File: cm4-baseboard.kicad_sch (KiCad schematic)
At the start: 4 parts

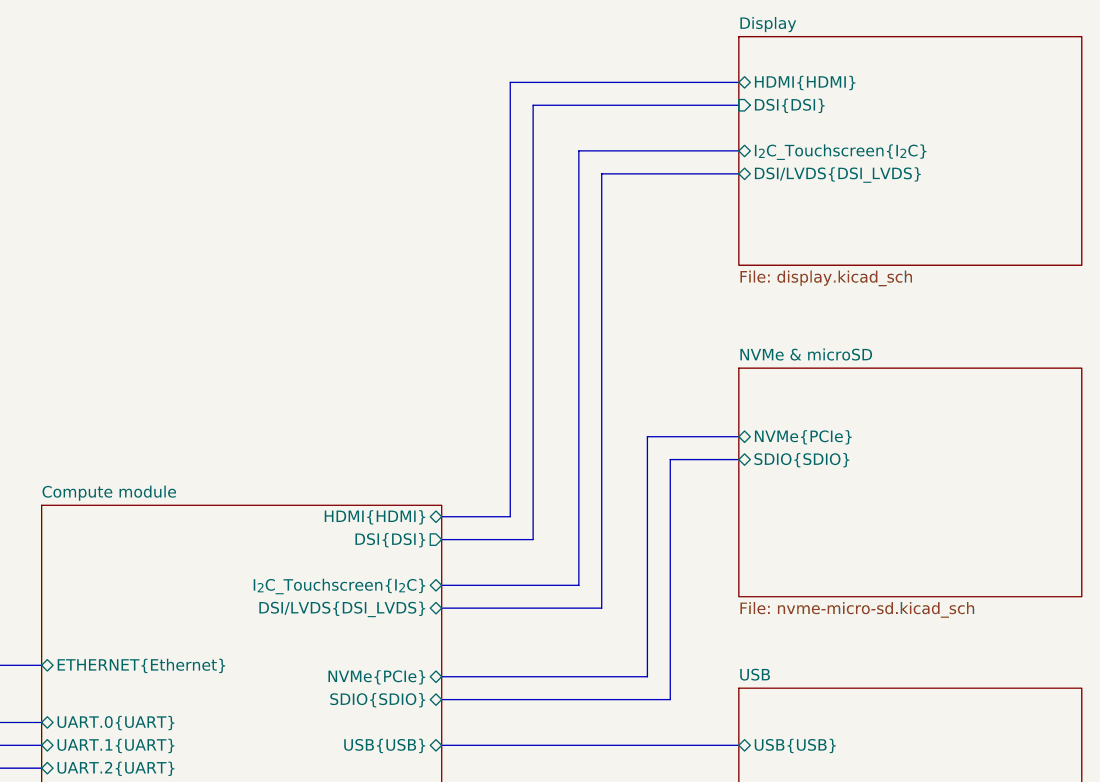
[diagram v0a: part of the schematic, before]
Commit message: [#54231] Rename bus DSI/LVDS to DisplayCtrl
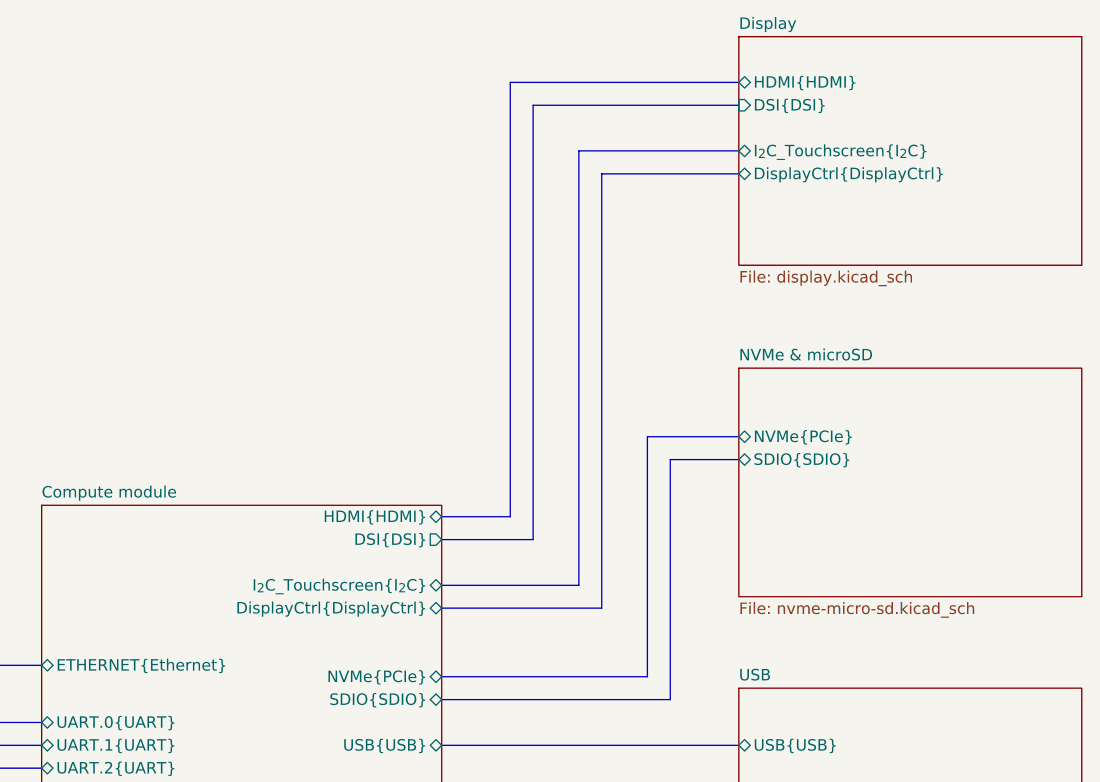
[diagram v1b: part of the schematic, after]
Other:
- sheet Compute module ports: added DisplayCtrl{DisplayCtrl}; removed DSI/LVDS{DSI_LVDS}
- sheet Display ports: added DisplayCtrl{DisplayCtrl}; removed DSI/LVDS{DSI_LVDS}
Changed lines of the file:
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@@
   (bus_alias "CSI" (members "D0_P" "D0_N" "D1_P" "D1_N" "D2_P" "D2_N" "D3_P" "D3_N" "CLK_P" "CLK_N"))
   (bus_alias "PCIe" (members "TX0_P" "TX0_N" "RX0_P" "RX0_N" "CLK_P" "CLK_N" "TX1_N" "TX2_N" "TX3_N" "TX1_P" "TX2_P" "TX3_P" "RX1_N" "RX2_N" "RX3_N" "RX1_P" "RX2_P" "RX3_P" "~{RST}" "~{CLK_REQ}"))
-  (bus_alias "HDMI" (members "D0_P" "D0_N" "D1_P" "D1_N" "D2_P" "D2_N" "CLK_P" "CLK_N" "SCL" "SDA" "CEC" "HPD"))
+  (bus_alias "SDIO" (members "D0" "D1" "D2" "D3" "CMD" "CLK" "CD"))
   (bus_alias "Ethernet" (members "D0_P" "D0_N" "D1_P" "D1_N" "D2_P" "D2_N" "D3_P" "D3_N" "LED_ACT" "LED_LINK"))
   (bus_alias "I_{2}C" (members "SCL" "SDA"))
-  (bus_alias "UART" (members "TX" "RX"))
   (bus_alias "USB" (members "RX_P" "RX_N" "TX_P" "TX_N" "D_P" "D_N"))
+  (bus_alias "HDMI" (members "D0_P" "D0_N" "D1_P" "D1_N" "D2_P" "D2_N" "CLK_P" "CLK_N" "SCL" "SDA" "CEC" "HPD"))
+  (bus_alias "UART" (members "TX" "RX"))
   (bus_alias "DSI" (members "D0_P" "D0_N" "D1_P" "D1_N" "D2_P" "D2_N" "D3_P" "D3_N" "CLK_P" "CLK_N"))
-  (bus_alias "SDIO" (members "D0" "D1" "D2" "D3" "CMD" "CLK" "CD"))
   (junction (at 166.37 264.16) (diameter 0) (color 0 0 0 0)
   )
@@
       (effects (font (size 1.27 1.27)) (justify right))
     )
-    (pin "DSI{slash}LVDS{DSI_LVDS}" bidirectional (at 243.84 113.03 0)
+    (pin "DisplayCtrl{DisplayCtrl}" bidirectional (at 243.84 113.03 0)
       (effects (font (size 1.27 1.27)) (justify right))
     )
@@
       (effects (font (size 1.27 1.27)) (justify left))
     )
-    (pin "DSI{slash}LVDS{DSI_LVDS}" bidirectional (at 276.86 64.77 180)
+    (pin "DisplayCtrl{DisplayCtrl}" bidirectional (at 276.86 64.77 180)
       (effects (font (size 1.27 1.27)) (justify left))
     )
@@
       (reference "#PWR?") (unit 1) (value "GND") (footprint "")
     )
-    (path "/b148dc70-7270-4ae3-80a1-580624d4cd31/5d61928f-81f0-4a4c-b452-b4734d3ec233/341a8429-1a92-49c6-adcc-ef7f1edcb952"
-      (reference "#PWR?") (unit 1) (value "GND") (footprint "")
-    )
     (path "/db597aea-6022-4be8-a5d9-f0f6712c4ff6/3813b611-ae52-4008-8362-850e3aa20b82"
       (reference "#PWR?") (unit 1) (value "GND") (footprint "")
@@
       (reference "#PWR?") (unit 1) (value "GND") (footprint "")
     )
-    (path "/b148dc70-7270-4ae3-80a1-580624d4cd31/5d61928f-81f0-4a4c-b452-b4734d3ec233/9a1114cc-d9e5-4f03-8637-8d3b91b40497"
-      (reference "#PWR?") (unit 1) (value "GND") (footprint "")
-    )
     (path "/00000000-0000-0000-0000-00005fea17c4/9cdec078-c17e-4daa-b8f1-7b28647f66b6"
       (reference "#PWR?") (unit 1) (value "+1V8") (footprint "")
@@
       (reference "C?") (unit 1) (value "C_template_name_0402") (footprint "antmicro-footprints:C_0402_1005Metric")
     )
+    (path "/b148dc70-7270-4ae3-80a1-580624d4cd31/5d61928f-81f0-4a4c-b452-b4734d3ec233/257eb24e-a684-4d63-8a65-0f0a78448243"
+      (reference "C?") (unit 1) (value "C_22u_25V_0805") (footprint "antmicro-footprints:C_0805_2012Metric")
+    )
     (path "/db597aea-6022-4be8-a5d9-f0f6712c4ff6/274e8c82-a4a9-46ce-bc84-d16e09bbd0c9"
       (reference "C?") (unit 1) (value "C_template_name_0402") (footprint "antmicro-footprints:C_0402_1005Metric")
@@
       (reference "C?") (unit 1) (value "C_330n_0603") (footprint "antmicro-footprints:C_0603_1608Metric")
     )
-    (path "/b148dc70-7270-4ae3-80a1-580624d4cd31/5d61928f-81f0-4a4c-b452-b4734d3ec233/453fe00b-ff52-4ef4-ba8f-d2d782db81e2"
-      (reference "C?") (unit 1) (value "C_10u_25V_0603") (footprint "antmicro-footprints:C_0603_1608Metric")
-    )
     (path "/00000000-0000-0000-0000-00005fea17e9/482637d7-45a3-440c-a11b-ab27ad2a09ba"
       (reference "C?") (unit 1) (value "C_22u_25V_0805") (footprint "antmicro-footprints:C_0805_2012Metric")
@@
       (reference "C?") (unit 1) (value "C_template_name_0402") (footprint "antmicro-footprints:C_0402_1005Metric")
     )
-    (path "/b148dc70-7270-4ae3-80a1-580624d4cd31/5d61928f-81f0-4a4c-b452-b4734d3ec233/5d833b9e-85a4-4a6f-8684-1cf9bdef1f01"
-      (reference "C?") (unit 1) (value "C_10u_25V_0603") (footprint "antmicro-footprints:C_0603_1608Metric")
-    )
-    (path "/b148dc70-7270-4ae3-80a1-580624d4cd31/5d61928f-81f0-4a4c-b452-b4734d3ec233/66dfef94-3e33-403a-b2be-3a327f56dc92"
-      (reference "C?") (unit 1) (value "C_10u_25V_0603") (footprint "antmicro-footprints:C_0603_1608Metric")
-    )
     (path "/00000000-0000-0000-0000-00005fea17e9/6b7d1f22-0be8-47c7-b016-6d7c031b8b41"
       (reference "C?") (unit 1) (value "C_22u_25V_0805") (footprint "antmicro-footprints:C_0805_2012Metric")
@@
       (reference "C?") (unit 1) (value "C_100n_0402") (footprint "antmicro-footprints:C_0402_1005Metric")
     )
-    (path "/b148dc70-7270-4ae3-80a1-580624d4cd31/5d61928f-81f0-4a4c-b452-b4734d3ec233/75197a1d-780f-46d2-9dce-65e41d058c74"
-      (reference "C?") (unit 1) (value "C_10u_25V_0603") (footprint "antmicro-footprints:C_0603_1608Metric")
-    )
     (path "/00000000-0000-0000-0000-00005fea17e9/780dfd9c-fc8c-4089-8330-e7de2f742555"
       (reference "C?") (unit 1) (value "C_22u_25V_0805") (footprint "antmicro-footprints:C_0805_2012Metric")
@@
       (reference "C?") (unit 1) (value "C_100n_0402") (footprint "antmicro-footprints:C_0402_1005Metric")
     )
+    (path "/b148dc70-7270-4ae3-80a1-580624d4cd31/5d61928f-81f0-4a4c-b452-b4734d3ec233/7b087682-4398-4ae5-9794-83c9bb11e283"
+      (reference "C?") (unit 1) (value "C_22u_25V_0805") (footprint "antmicro-footprints:C_0805_2012Metric")
+    )
     (path "/b148dc70-7270-4ae3-80a1-580624d4cd31/5d61928f-81f0-4a4c-b452-b4734d3ec233/80d05272-f4bc-4c0b-b517-a6d34f4a8421"
       (reference "C?") (unit 1) (value "C_1u_25V_0402") (footprint "antmicro-footprints:C_0402_1005Metric")
@@
       (reference "C?") (unit 1) (value "C_10p_0402") (footprint "antmicro-footprints:C_0402_1005Metric")
     )
+    (path "/b148dc70-7270-4ae3-80a1-580624d4cd31/5d61928f-81f0-4a4c-b452-b4734d3ec233/87418403-96e0-4834-9247-2518b8abc38b"
+      (reference "C?") (unit 1) (value "C_22u_25V_0805") (footprint "antmicro-footprints:C_0805_2012Metric")
+    )
     (path "/db597aea-6022-4be8-a5d9-f0f6712c4ff6/88d5e9a9-c2b1-463d-919b-768178eb5b8b"
       (reference "C?") (unit 1) (value "C_100n_0402") (footprint "antmicro-footprints:C_0402_1005Metric")
@@
       (reference "C?") (unit 1) (value "C_10n_0402") (footprint "antmicro-footprints:C_0402_1005Metric")
     )
-    (path "/b148dc70-7270-4ae3-80a1-580624d4cd31/5d61928f-81f0-4a4c-b452-b4734d3ec233/ba404e87-ab9c-4537-886b-3e04a5eb8c72"
-      (reference "C?") (unit 1) (value "C_22u_16V_0603") (footprint "antmicro-footprints:C_0603_1608Metric")
-    )
     (path "/00000000-0000-0000-0000-00005fea17e9/bc26d64c-8cd8-4a33-894b-b2b889e6c4f9"
       (reference "C?") (unit 1) (value "C_22u_25V_0805") (footprint "antmicro-footprints:C_0805_2012Metric")
@@
       (reference "C?") (unit 1) (value "C_220n_16V_0402") (footprint "antmicro-footprints:C_0402_1005Metric")
     )
+    (path "/b148dc70-7270-4ae3-80a1-580624d4cd31/5d61928f-81f0-4a4c-b452-b4734d3ec233/e050934f-2e7f-4d1d-a6b0-f09cd3270d46"
+      (reference "C?") (unit 1) (value "C_22u_25V_0805") (footprint "antmicro-footprints:C_0805_2012Metric")
+    )
     (path "/db597aea-6022-4be8-a5d9-f0f6712c4ff6/e5121825-db13-4ea1-a393-845e0e43bef6"
       (reference "C?") (unit 1) (value "C_template_name_0402") (footprint "antmicro-footprints:C_0402_1005Metric")
@@
       (reference "L1") (unit 1) (value "L_1u8_14A_Coilcraft-XAL6030") (footprint "antmicro-footprints:L_Coilcraft-XAL6030")
     )
+    (path "/b148dc70-7270-4ae3-80a1-580624d4cd31/5d61928f-81f0-4a4c-b452-b4734d3ec233/2db4c736-e13c-47a7-9ea7-9867d69cfe2b"
+      (reference "L?") (unit 1) (value "L_15u_2.8A_Coilcraft-XAL4040") (footprint "antmicro-footprints:L_Coilcraft-XAL4040")
+    )
     (path "/00000000-0000-0000-0000-00005fea17e9/379854a8-c5e4-44ac-bfdb-4f3a8f72b89e"
       (reference "L?") (unit 1) (value "L_1u_5.5A_SRP3212") (footprint "antmicro-footprints:L_Bourns-SRP3212A")
@@
       (reference "L?") (unit 1) (value "L_template_name") (footprint "antmicro-footprints:")
     )
-    (path "/b148dc70-7270-4ae3-80a1-580624d4cd31/5d61928f-81f0-4a4c-b452-b4734d3ec233/be115923-ae26-4b90-8620-7915e23bf03c"
-      (reference "L?") (unit 1) (value "L_27u_2A_Bourns-SRP6540") (footprint "antmicro-footprints:L_Bourns-SRP6540")
-    )
     (path "/b148dc70-7270-4ae3-80a1-580624d4cd31/5d61928f-81f0-4a4c-b452-b4734d3ec233/fbd03150-a37a-4595-a068-06ae25c3fd31"
       (reference "L?") (unit 1) (value "L_3u3_2.5A_1008") (footprint "antmicro-footprints:L_1008_2520Metric")
@@
       (reference "R?") (unit 1) (value "R_10k_0402") (footprint "antmicro-footprints:R_0402_1005Metric")
     )
-    (path "/b148dc70-7270-4ae3-80a1-580624d4cd31/5d61928f-81f0-4a4c-b452-b4734d3ec233/712ea8e9-a2fd-47ff-9417-0767f670e33a"
-      (reference "R?") (unit 1) (value "R_100k_0402") (footprint "antmicro-footprints:R_0402_1005Metric")
-    )
     (path "/b148dc70-7270-4ae3-80a1-580624d4cd31/7832ee62-288d-4a3e-80f4-f13d1b9ce12b/7a4b7e10-3a15-4ce0-adf9-c5b9efa631ad"
